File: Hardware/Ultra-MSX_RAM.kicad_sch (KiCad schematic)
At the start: 10 parts, among them J10 Micro_SD_Card_Det_GCT, J9 Conn_SO-DIMM-144, U10 SST39SF040, U8 AS6C8008-55ZIN

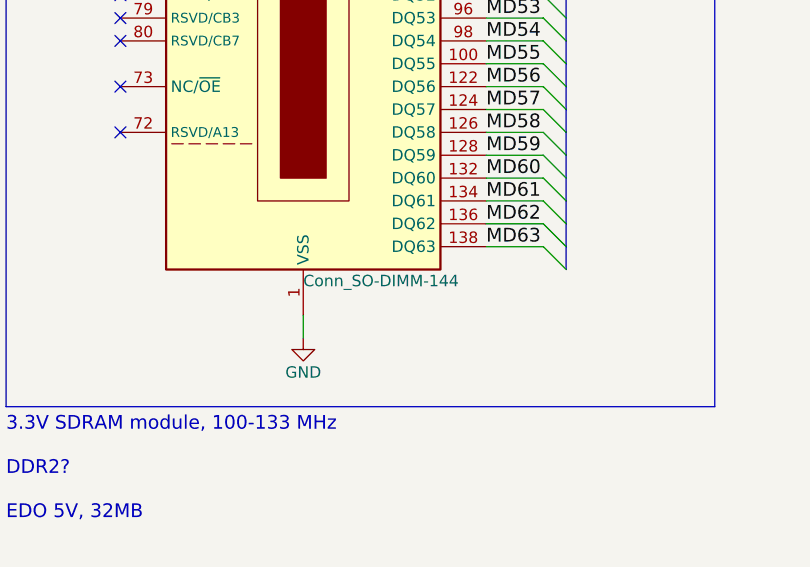
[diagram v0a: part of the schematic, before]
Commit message: Added a 3D-model for the SDRAM-module. Prepping the design for a fork using a single, more modern FPGA.
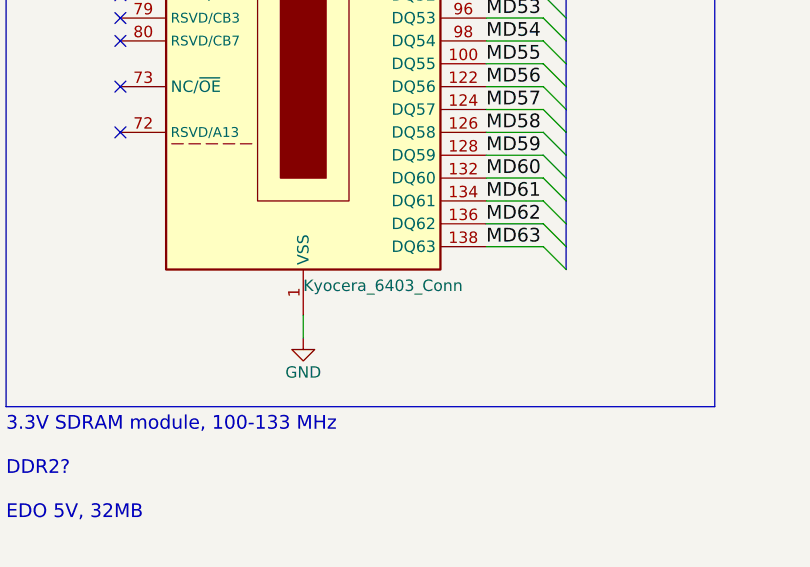
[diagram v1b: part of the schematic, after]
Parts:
- J9: value Conn_SO-DIMM-144 -> Kyocera_6403_Conn; footprint LRJ:SODIMM-144_socket -> LRJ:Kyocera_296403144121856+; symbol LRJ-parts:Conn_SO-DIMM-144 -> LRJ-parts:Kyocera_296403144221856A+; Current rating (none) -> 0.3A; MPN n/a -> 296403144221856A+; Manufacturer n/a -> Kyocera/AVX; Operating temperature (none) -> -55 C ~ +85 C; Status (none) -> OBSOLETE; Voltage rating (none) -> 25V
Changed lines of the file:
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@@
     )
   )
-  (symbol (lib_id "LRJ-parts:Conn_SO-DIMM-144") (at 166.37 118.11 0) (unit 1)
+  (symbol (lib_id "LRJ-parts:Kyocera_296403144221856A+") (at 166.37 118.11 0) (unit 1)
     (in_bom yes) (on_board yes) (dnp no)
     (property "Reference" "J9" (at 167.64 38.1 0)
       (effects (font (size 1.27 1.27)) (justify left))
     )
-    (property "Value" "Conn_SO-DIMM-144" (at 166.37 205.74 0)
-      (effects (font (size 1.27 1.27)) (justify left))
+    (property "Value" "Kyocera_6403_Conn" (at 166.37 207.01 0)
+      (effects (font (size 1.27 1.27)) (justify left bottom))
     )
-    (property "Footprint" "LRJ:SODIMM-144_socket" (at 179.07 209.55 0)
+    (property "Footprint" "LRJ:Kyocera_296403144121856+" (at 179.07 209.55 0)
       (effects (font (size 1.27 1.27)) hide)
     )
-    (property "Datasheet" "https://pinoutguide.com/Memory/SimmSo144_pinout.shtml" (at 229.87 115.57 0)
+    (property "Datasheet" "https://www.mouser.se/datasheet/2/40/6403-3180434.pdf" (at 229.87 115.57 0)
       (effects (font (size 1.27 1.27)) hide)
     )
-    (property "MPN" "n/a" (at 204.47 105.41 0)
+    (property "MPN" "296403144221856A+" (at 212.09 113.03 0)
       (effects (font (size 1.27 1.27)) hide)
     )
-    (property "Manufacturer" "n/a" (at 204.47 107.95 0)
+    (property "Manufacturer" "Kyocera/AVX" (at 209.55 102.87 0)
       (effects (font (size 1.27 1.27)) hide)
     )
@@
       (effects (font (size 1.27 1.27)) hide)
     )
+    (property "Current rating" "0.3A" (at 204.47 107.95 0)
+      (effects (font (size 1.27 1.27)) hide)
+    )
+    (property "Operating temperature" "-55 C ~ +85 C" (at 209.55 110.49 0)
+      (effects (font (size 1.27 1.27)) hide)
+    )
+    (property "Status" "OBSOLETE" (at 207.01 120.65 0)
+      (effects (font (size 1.27 1.27)) hide)
+    )
+    (property "Voltage rating" "25V" (at 204.47 105.41 0)
+      (effects (font (size 1.27 1.27)) hide)
+    )

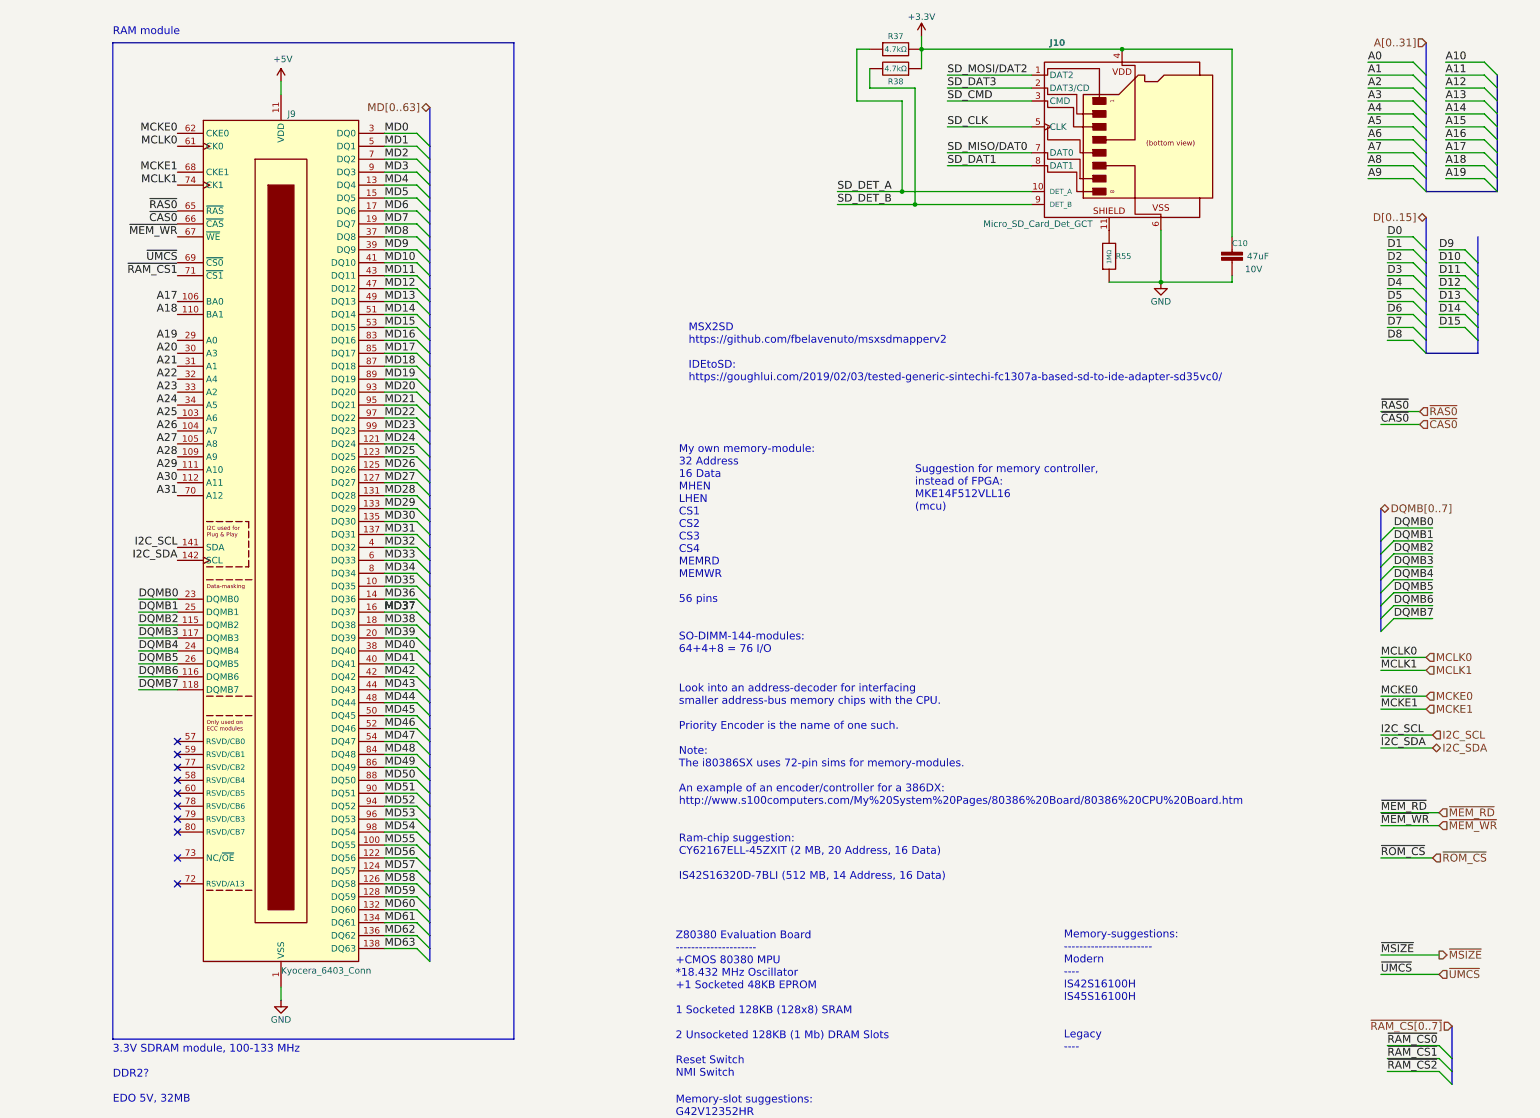
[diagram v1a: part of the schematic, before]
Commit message: Returned to Simm-72 memory module to simplify design, returned to AT40K40 with 254 io, FPGA.
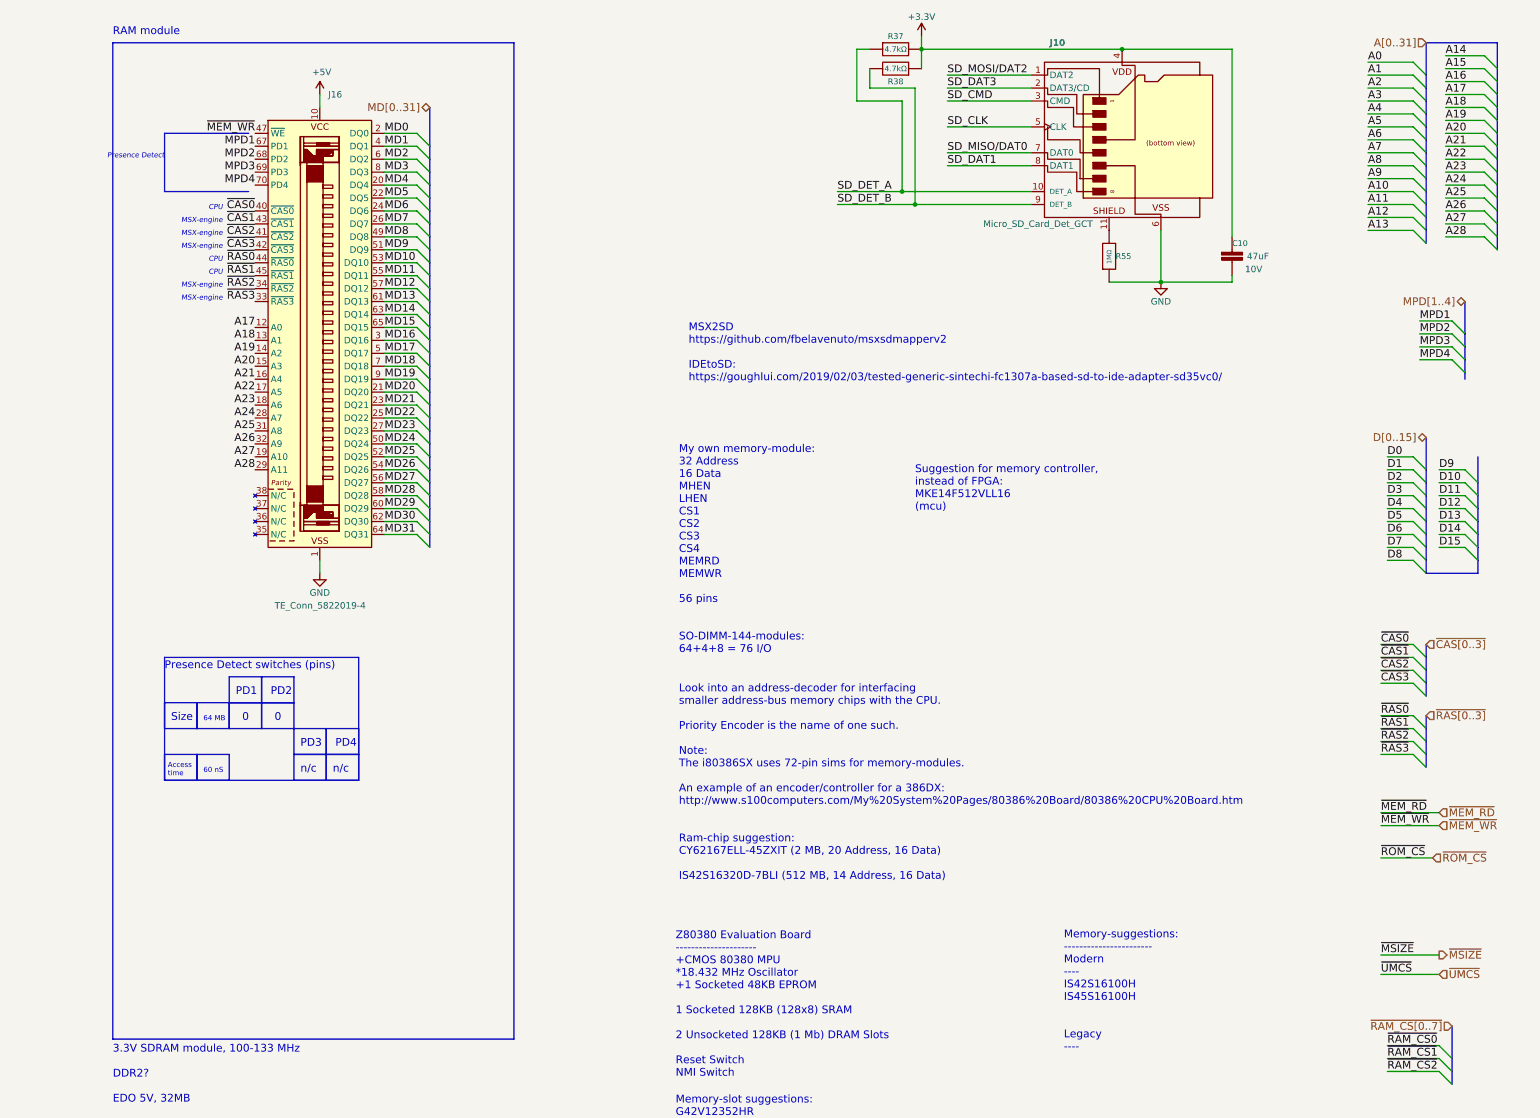
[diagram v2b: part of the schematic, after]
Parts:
- removed J9: Kyocera_6403_Conn, LRJ:Kyocera_296403144121856+, symbol LRJ-parts:Kyocera_296403144221856A+
- added J16: TE_Conn_5822019-4, LRJ:SIMM-72_socket, symbol LRJ-parts:TE_Conn_5822019-4
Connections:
- net +5V: now also J16.10 (VCC), J16.30 (VCC), J16.59 (VCC)
- net A17: now also J16.12 (A0)
- net A18: now also J16.13 (A1)
- net A19: now also J16.14 (A2)
- net A20: now also J16.15 (A3)
- net A21: now also J16.16 (A4)
- net A22: now also J16.17 (A5)
- net A23: now also J16.18 (A6)
- net A24: now also J16.28 (A7)
- net A25: now also J16.31 (A8)
- net A26: now also J16.32 (A9)
- net A27: now also J16.19 (A10)
- net A28: now also J16.29 (A11)
- net GND: now also J16.1 (VSS), J16.39 (VSS), J16.72 (VSS)
- net MD0: now also J16.2 (DQ0)
- net MD1: now also J16.4 (DQ1)
- net MD10: now also J16.53 (DQ10)
- net MD11: now also J16.55 (DQ11)
- net MD12: now also J16.57 (DQ12)
- net MD13: now also J16.61 (DQ13)
- net MD14: now also J16.63 (DQ14)
- net MD15: now also J16.65 (DQ15)
- net MD16: now also J16.3 (DQ16)
- net MD17: now also J16.5 (DQ17)
- net MD18: now also J16.7 (DQ18)
- net MD19: now also J16.9 (DQ19)
- net MD2: now also J16.6 (DQ2)
- net MD20: now also J16.21 (DQ20)
- net MD21: now also J16.23 (DQ21)
- net MD22: now also J16.25 (DQ22)
- net MD23: now also J16.27 (DQ23)
- net MD24: now also J16.50 (DQ24)
- net MD25: now also J16.52 (DQ25)
- net MD26: now also J16.54 (DQ26)
- net MD27: now also J16.56 (DQ27)
- net MD28: now also J16.58 (DQ28)
- net MD29: now also J16.60 (DQ29)
- net MD3: now also J16.8 (DQ3)
- net MD30: now also J16.62 (DQ30)
- net MD31: now also J16.64 (DQ31)
- net MD4: now also J16.20 (DQ4)
- net MD5: now also J16.22 (DQ5)
- net MD6: now also J16.24 (DQ6)
- net MD7: now also J16.26 (DQ7)
- net MD8: now also J16.49 (DQ8)
- net MD9: now also J16.51 (DQ9)
- net ~{CAS0}: now also J16.40 (~{CAS0})
- net ~{MEM_WR}: now also J16.47 (~{WE})
- net ~{RAS0}: now also J16.44 (~{RAS0})
- new net MPD1: J16.67 (PD1)
- new net MPD2: J16.68 (PD2)
- new net MPD3: J16.69 (PD3)
- new net MPD4: J16.70 (PD4)
- new net ~{CAS1}: J16.43 (~{CAS1})
- new net ~{CAS2}: J16.41 (~{CAS2})
- new net ~{CAS3}: J16.42 (~{CAS3})
- new net ~{RAS1}: J16.45 (~{RAS1})
- new net ~{RAS2}: J16.34 (~{RAS2})
- new net ~{RAS3}: J16.33 (~{RAS3})
- no-connect marks 10 -> 0
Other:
- note added: "0"
- note added: "60 nS"
- note added: "64 MB"
- note added: "Access time"
- note added: "CPU"
- note added: "MSX-engine"
- note added: "PD1 PD2"
- note added: "PD3 PD4"
- note added: "Presence Detect"
- note added: "Presence Detect switches (pins)"
- note added: "Size"
- note added: "n/c"
